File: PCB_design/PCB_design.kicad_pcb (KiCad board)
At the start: 2 copper layers, 39 parts, among them J1 USB_B_Micro, J4 Conn_01x02_Pin, Q1 FS8205A, U1 L298N, U2 L7805, U3 TP4056, U4 DW01A

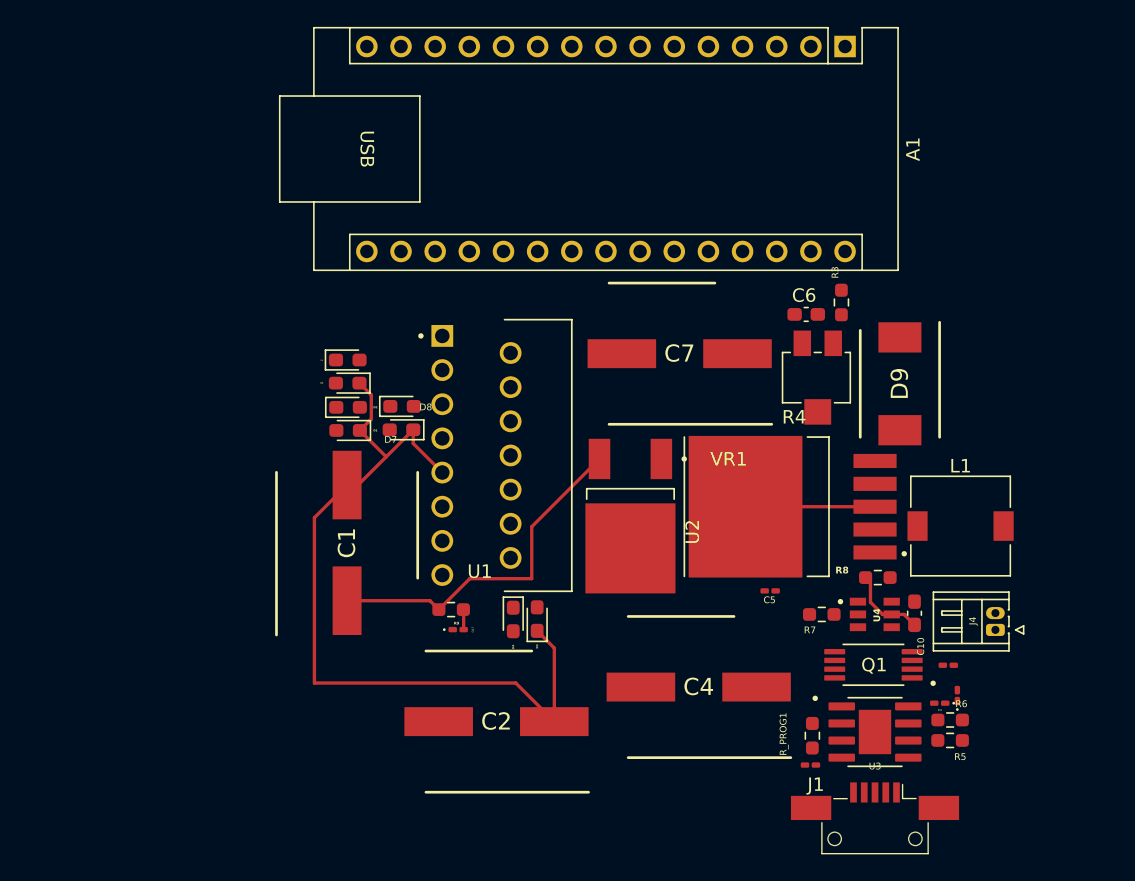
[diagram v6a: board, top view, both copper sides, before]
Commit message: Fix errors on circuit schematic and reorder PCB layout
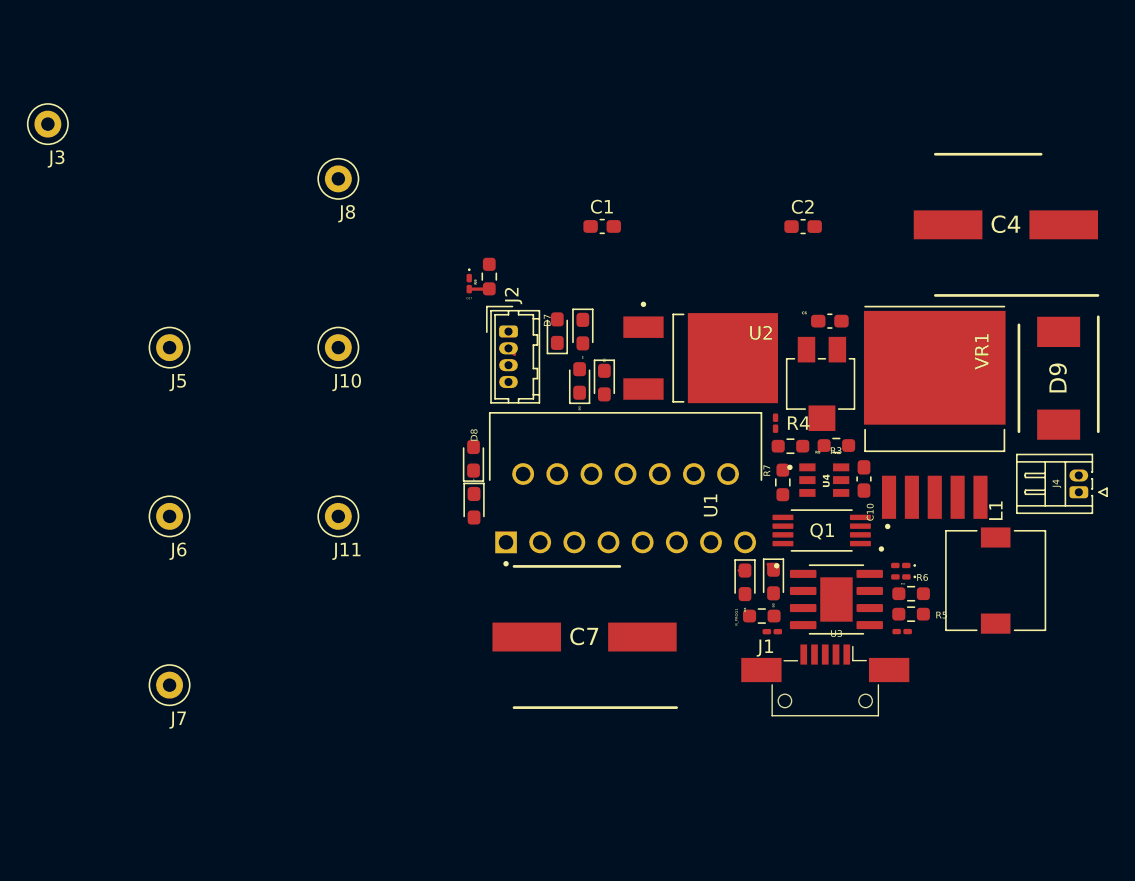
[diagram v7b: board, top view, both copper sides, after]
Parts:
- removed A1: Arduino_Nano_v2.x, Module:Arduino_Nano
- added J10: Conn_01x01_Socket, TestPoint:TestPoint_Loop_D1.80mm_Drill1.0mm_Beaded, F.Cu at (128.9, 70.2)
- added J11: Conn_01x01_Socket, TestPoint:TestPoint_Loop_D1.80mm_Drill1.0mm_Beaded, F.Cu at (128.9, 82.8)
- added J2: Conn_01x04_Socket, Connector_Hirose:Hirose_DF13-04P-1.25DSA_1x04_P1.25mm_Vertical, F.Cu at (141.6, 69.0)
- added J3: Conn_01x01_Socket, TestPoint:TestPoint_Loop_D1.80mm_Drill1.0mm_Beaded, F.Cu at (107.3, 53.6)
- added J5: Conn_01x01_Socket, TestPoint:TestPoint_Loop_D1.80mm_Drill1.0mm_Beaded, F.Cu at (116.4, 70.2)
- added J6: Conn_01x01_Socket, TestPoint:TestPoint_Loop_D1.80mm_Drill1.0mm_Beaded, F.Cu at (116.4, 82.8)
- added J7: Conn_01x01_Socket, TestPoint:TestPoint_Loop_D1.80mm_Drill1.0mm_Beaded, F.Cu at (116.4, 95.3)
- added J8: Conn_01x01_Socket, TestPoint:TestPoint_Loop_D1.80mm_Drill1.0mm_Beaded, F.Cu at (128.9, 57.7)
- C1, C2: value 220uF -> 10uF; footprint Capacitor_220uF35V_smaller:CAPAE1050X1050N -> Capacitor_SMD:C_0603_1608Metric_Pad1.08x0.95mm_HandSolder
- moved C2 43.3 mm to (163.5, 61.2), turned to 0 degrees
- moved C4 41.3 mm to (178.6, 61.1)
- moved D2 34.2 mm to (161.3, 87.6), turned to -90 degrees
- moved C1 30.2 mm to (148.5, 61.2), turned to 0 degrees
- moved D17 25.7 mm to (138.7, 65.5), turned to -90 degrees
- moved R9 24.9 mm to (140.1, 64.9), turned to -90 degrees
- moved C7 22.2 mm to (147.2, 91.7)
- moved D1 19.4 mm to (148.7, 72.8), turned to -90 degrees
- moved D3 18.0 mm to (146.9, 72.7)
- moved D5 17.9 mm to (147.1, 69.0), turned to -90 degrees
- moved D4 17.5 mm to (159.2, 87.7)
- moved U1 16.1 mm to (141.4, 84.7), turned to 90 degrees
- moved D6 14.3 mm to (139.0, 82.0), turned to -90 degrees
- moved D7 13.7 mm to (145.2, 69.0), turned to 90 degrees
- moved U2 12.9 mm to (155.9, 71.0), turned to 0 degrees
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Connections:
- C1 pad 1: Net-(U2-OUT) -> +5V Arduino
- C1 pad 2: Net-(D1-K) -> GND_Arduino1
- C2 pad 1: Net-(D1-K) -> Boost_Out
- C2 pad 2: GND_Out -> GND_Arduino1
- C4 pad 2: GND_Out -> GND_Arduino1
- C5 pad 2: GND_Out -> GND_Arduino1
- C6 pad 2: GND_Out -> GND_Arduino1
- C7 pad 2: GND_Out -> GND_Arduino1
- C8 pad 2: GND_Out -> GND_Arduino1
- C9 pad 2: GND_Out -> GND_Arduino1
- D1 pad 1: Net-(D1-K) -> Boost_Out
- D17 pad 1: GND_Out -> GND_Arduino1
- D2 pad 2: GND_Out -> GND_Arduino1
- D3 pad 1: Net-(D1-K) -> Boost_Out
- D4 pad 2: GND_Out -> GND_Arduino1
- D5 pad 1: Net-(D1-K) -> Boost_Out
- D6 pad 2: GND_Out -> GND_Arduino1
- D7 pad 1: Net-(D1-K) -> Boost_Out
- D8 pad 2: GND_Out -> GND_Arduino1
- J1 pad 5: GND_Out -> GND_Arduino1
- Q1 pad 6: GND_Out -> GND_Arduino1
- Q1 pad 7: GND_Out -> GND_Arduino1
- R3 pad 2: GND_Out -> GND_Arduino1
- R7 pad 2: GND_Out -> GND_Arduino1
- R9 pad 1: Net-(U2-OUT) -> +5V Arduino
- R_PROG1 pad 2: GND_Out -> GND_Arduino1
- U1 pad 1: GND_Out -> GND_Arduino1
- U1 pad 10: Net-(A1-A2) -> A2
- U1 pad 11: +5V -> +5V Arduino
- U1 pad 12: Net-(A1-A3) -> A3
- U1 pad 15: GND_Out -> GND_Arduino1
- U1 pad 5: Net-(A1-A0) -> A0
- U1 pad 6: +5V -> +5V Arduino
- U1 pad 7: Net-(A1-A1) -> A1
- U1 pad 8: GND_Out -> GND_Arduino1
- U1 pad 9: Net-(D1-K) -> +5V Arduino
- U2 pad 2: GND_Out -> GND_Arduino1
- U2 pad 3: Net-(U2-OUT) -> +5V Arduino
- U3 pad 1: GND_Out -> GND_Arduino1
- U3 pad 3: GND_Out -> GND_Arduino1
- U3 pad 9: GND_Out -> GND_Arduino1
- VR1 pad 1: GND_Out -> GND_Arduino1
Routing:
- net Net-(D1-K): track 59.7 -> 0.00 mm
- net Net-(U2-OUT): track 25.9 -> 0.00 mm
- net Net-(D9-B): track 11.0 -> 0.00 mm
- net Net-(U4-VCC): track 5.95 -> 0.00 mm
- net OUT3: track 0.00 -> 0.86 mm
- net OUT2: track 0.00 -> 0.63 mm
- net OUT4: track 0.00 -> 0.57 mm
- net Boost_Out: track 0.00 -> 0.56 mm

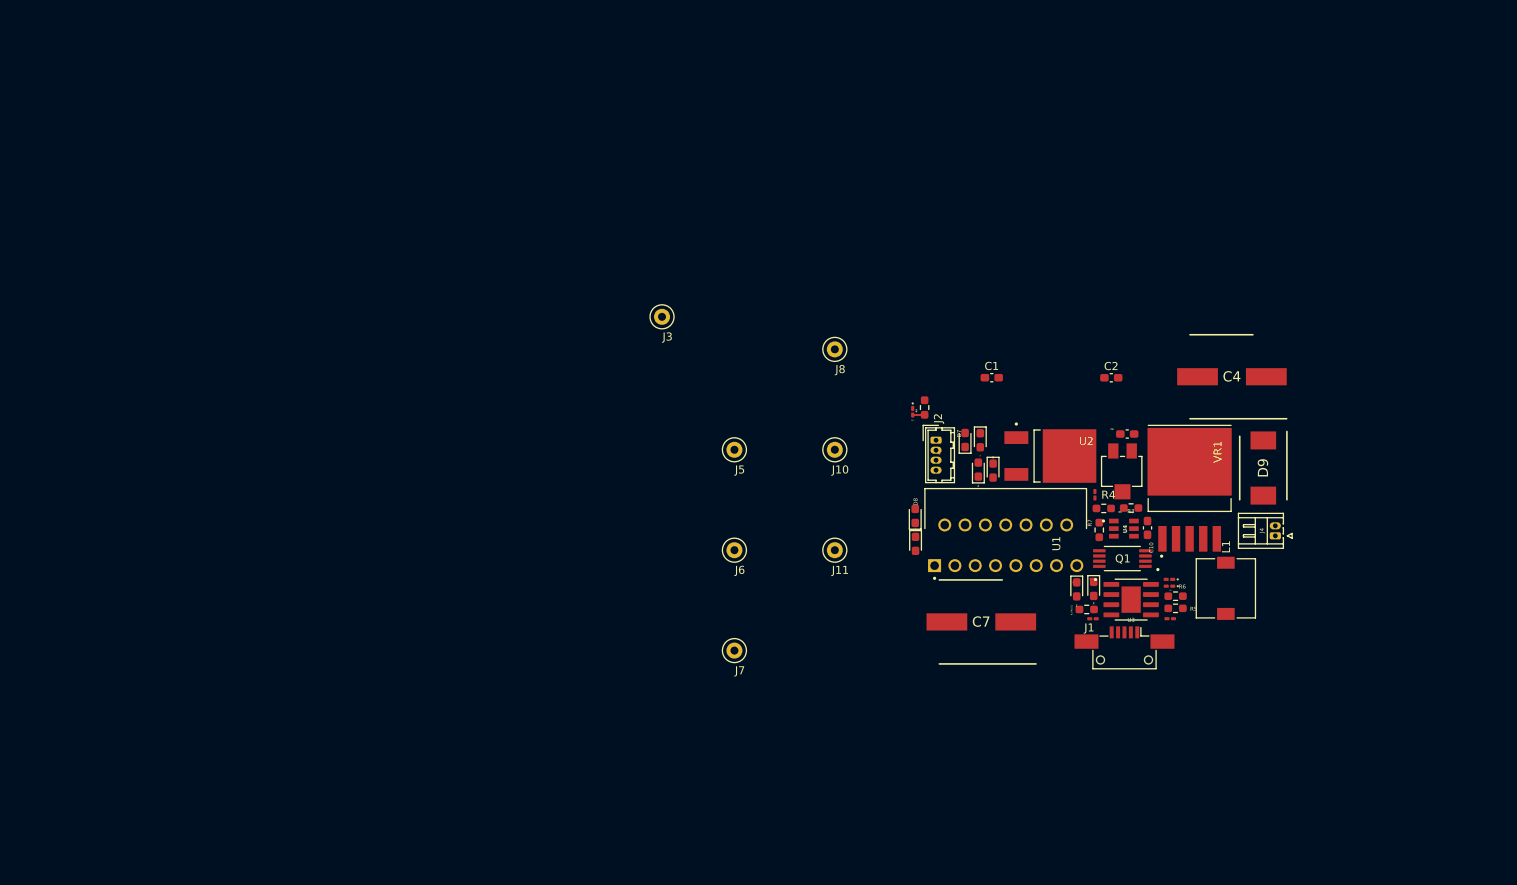
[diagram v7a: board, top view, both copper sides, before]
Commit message: Finished PCB design and outline, added interactive html design
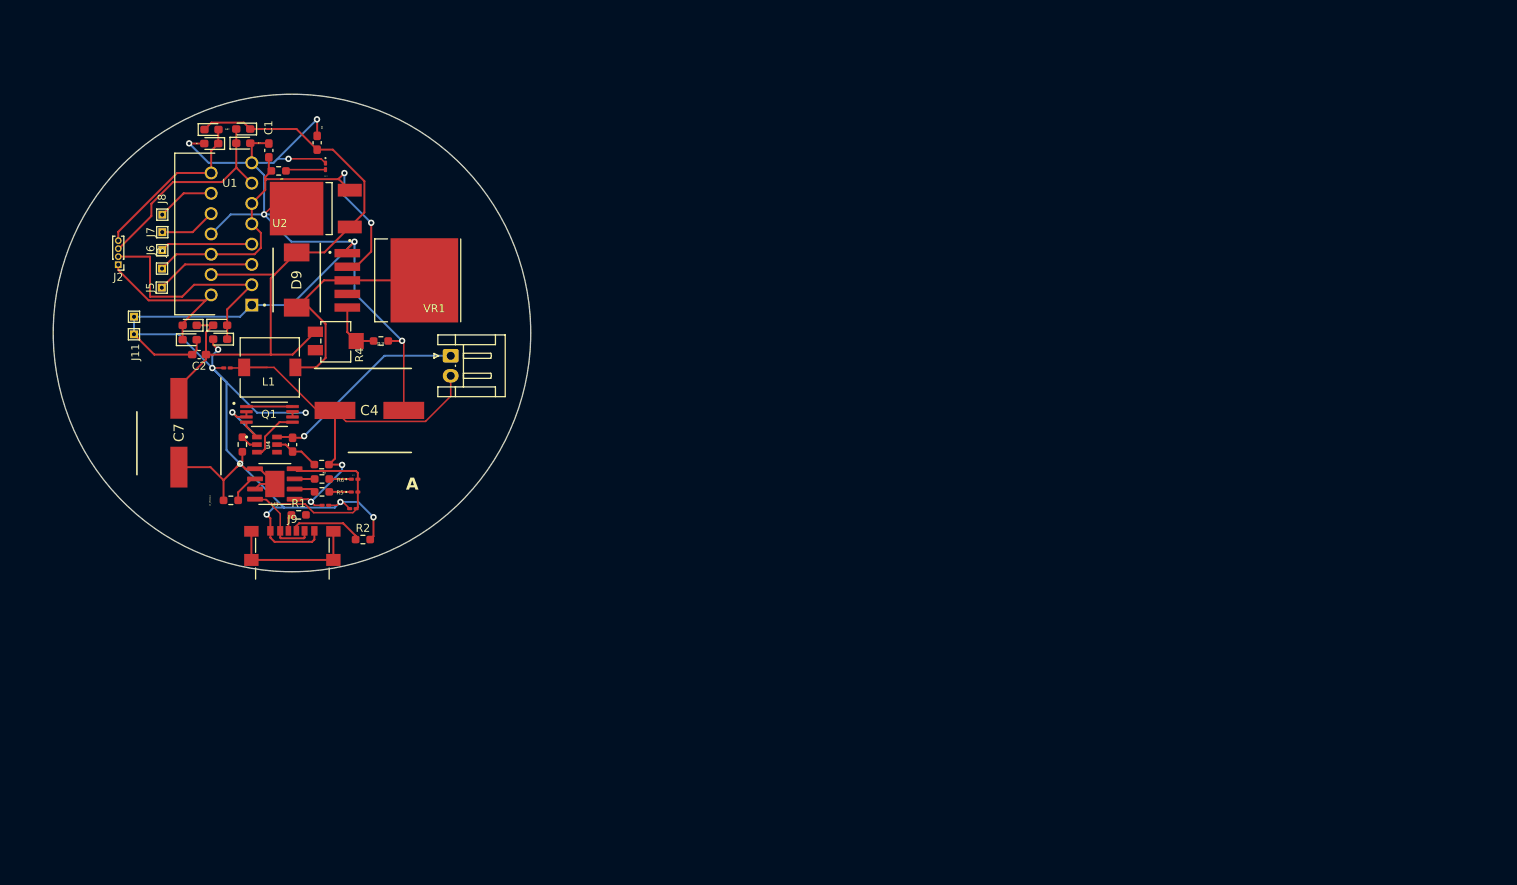
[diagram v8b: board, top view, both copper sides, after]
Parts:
- removed J1: USB_B_Micro, Connector_USB:USB_Mini-B_AdamTech_MUSB-B5-S-VT-TSMT-1_SMD_Vertical
- added J9: USB_C_Receptacle_PowerOnly_6P, Connector_USB:USB_C_Receptacle_GCT_USB4135-GF-A_6P_TopMnt_Horizontal, F.Cu at (61.1, 83.4)
- added R1: 5.2k, Resistor_SMD:R_0603_1608Metric_Pad0.98x0.95mm_HandSolder, F.Cu at (61.9, 78.4)
- added R2: 5.2k, Resistor_SMD:R_0603_1608Metric_Pad0.98x0.95mm_HandSolder, F.Cu at (69.9, 81.4)
- C4: value C_Polarized_US -> 47uF/50V
- C5, C6: value C_Polarized_US -> 1uF
- C7: value C_Polarized_US -> 220uF/50V
- J10, J11, J3, J5, J6, J7, J8: footprint TestPoint:TestPoint_Loop_D1.80mm_Drill1.0mm_Beaded -> TestPoint:TestPoint_THTPad_1.0x1.0mm_Drill0.5mm
- J2: footprint Connector_Hirose:Hirose_DF13-04P-1.25DSA_1x04_P1.25mm_Vertical -> Connector_PinHeader_1.00mm:PinHeader_1x04_P1.00mm_Vertical
- J4: footprint Connector_Hirose:Hirose_DF13-02P-1.25DS_1x02_P1.25mm_Horizontal -> Connector_JST:JST_EH_S2B-EH_1x02_P2.50mm_Horizontal
- moved D2 123.6 mm to (51.0, 31.9), turned to 180 degrees
- moved D9 123.1 mm to (61.6, 49.0)
- moved L1 122.7 mm to (58.3, 59.9), turned to 0 degrees
- moved D4 118.2 mm to (55.0, 31.9), turned to 0 degrees
- moved C2 114.1 mm to (49.5, 58.3), turned to 180 degrees
- moved C5 109.6 mm to (52.9, 60.0), turned to 180 degrees
- moved Q1 108.1 mm to (58.2, 65.8), turned to 0 degrees
- moved U3 108.0 mm to (58.9, 74.5)
- moved C4 107.9 mm to (70.7, 65.3), turned to 0 degrees
- moved R_PROG1 107.9 mm to (53.4, 76.5), turned to 180 degrees
- moved R6 107.7 mm to (64.8, 73.9)
- moved R5 107.7 mm to (64.8, 75.5)
- moved R7 107.6 mm to (54.9, 69.6), turned to -90 degrees
- moved U4 107.6 mm to (57.9, 69.6)
- moved C6 107.6 mm to (64.2, 31.8), turned to 90 degrees
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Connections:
- VR1 pad 2: unconnected-(VR1-EN-Pad2) -> +5V Arduino
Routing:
- net GND_Arduino1: track 0.00 -> 245.9 mm, vias 0 -> 13
- net Boost_Out: track 0.56 -> 87.9 mm
- net Bat+: track 0.00 -> 54.1 mm, vias 0 -> 2
- net +5V Arduino: track 0.00 -> 53.8 mm, vias 0 -> 2
- net Net-(D10-A): track 0.00 -> 35.7 mm
- net Batt-: track 0.00 -> 32.8 mm, vias 0 -> 2
- net Net-(D9-B): track 0.00 -> 30.3 mm
- net OUT2: track 0.63 -> 30.4 mm
- net OUT3: track 0.86 -> 27.4 mm
- net OUT4: track 0.57 -> 21.5 mm
- net OUT1: track 0.37 -> 20.5 mm
- net unconnected-(J9-SHIELD-PadS1): track 0.00 -> 17.4 mm
- net A0: track 0.00 -> 12.5 mm
- net A1: track 0.00 -> 11.5 mm
- net Net-(J9-CC2): track 0.00 -> 9.27 mm
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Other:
- board outline added: 59.7 x 59.7 mm
- board text added: "A"
